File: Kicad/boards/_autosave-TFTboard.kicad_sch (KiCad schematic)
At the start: 24 parts, among them J1 5051104096, J10 Conn_01x04, J13 Conn_01x03 speaker, J3 URM37, J4 Conn_01x03 servo, J5 RS485_TFT, J6 Conn_01x03 encoder_direct, SW1 SW_DIP_x01, U1 MOUDLE-SEEEDUINO-XIAO-ESP32C3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, U11 MOUDLE-SEEEDUINO-XIAO-ESP32C3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

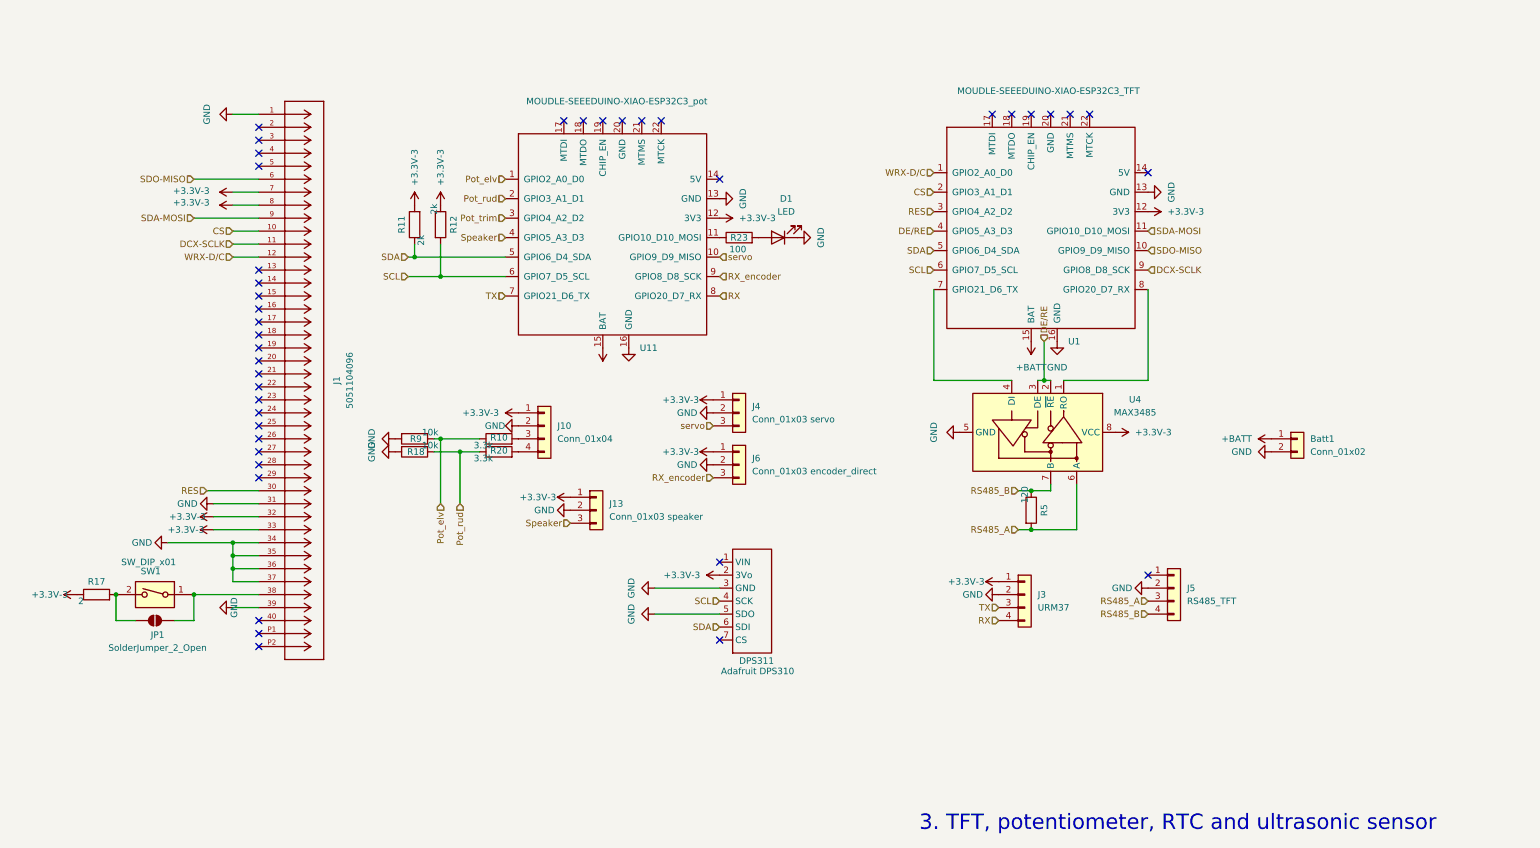
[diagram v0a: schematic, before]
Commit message: 電源1つに
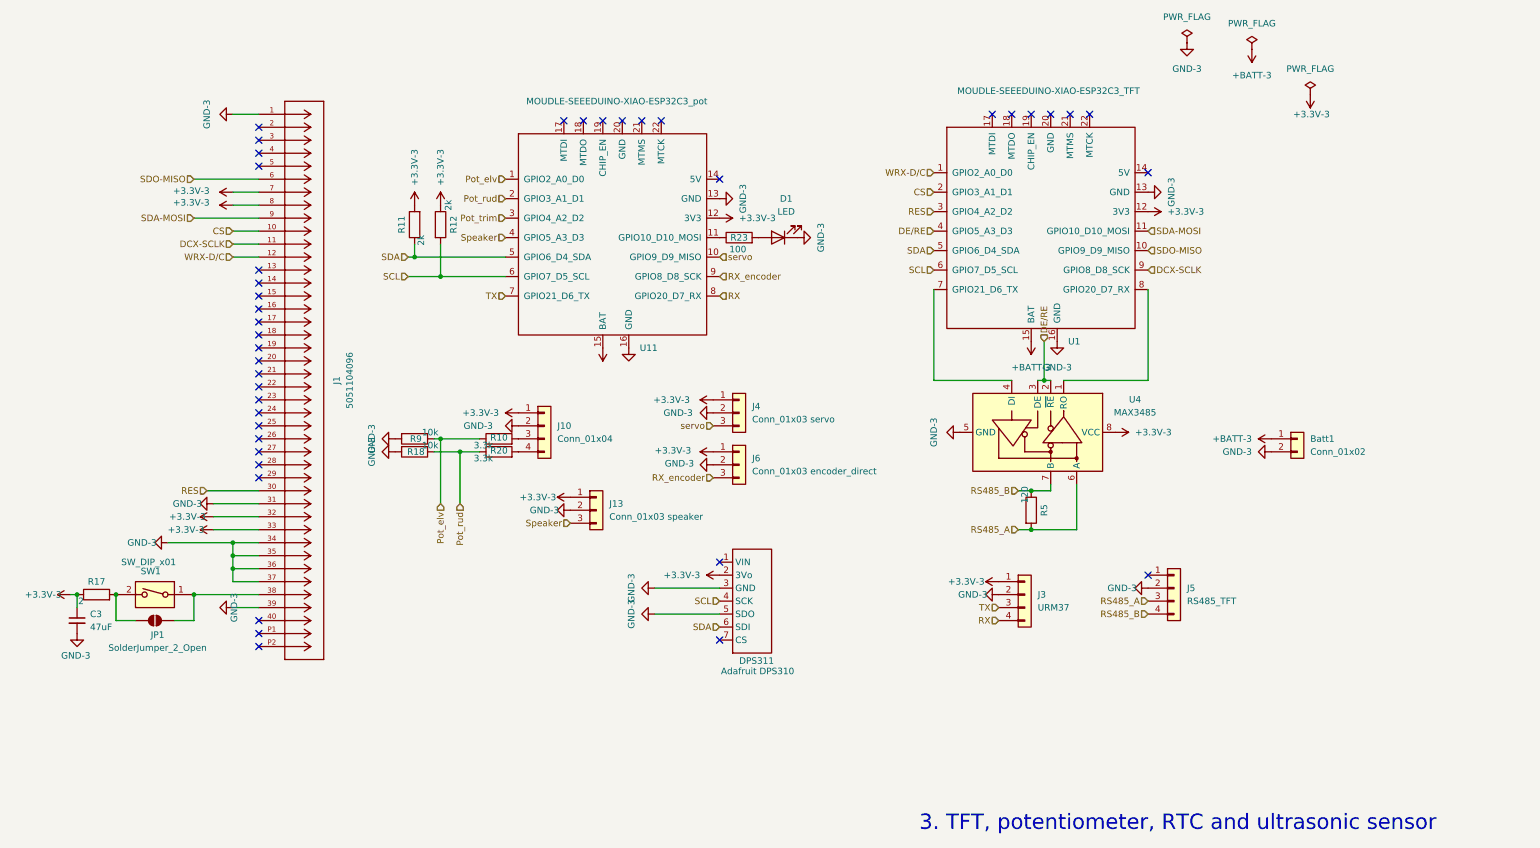
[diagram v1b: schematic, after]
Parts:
- added C3: 47uF, Capacitor_SMD:C_0603_1608Metric_Pad1.08x0.95mm_HandSolder, symbol Device:C_Small
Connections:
- net +3.3V-3: now also C3.1
- net +BATT renamed +BATT-3
- net GND renamed GND-3
- net GND-3: now also C3.2
